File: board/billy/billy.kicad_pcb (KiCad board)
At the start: 2 copper layers, 70 x 50 mm, 83 parts, among them J1 Screw_Terminal_01x02, J10 Screw_Terminal_01x02, J11 Screw_Terminal_01x03, J12 USB_B_Micro, J2 Conn_01x06, J3 Screw_Terminal_01x02, J4 Screw_Terminal_01x02, J5 Conn_01x02, J6 Conn_01x03, J7 Screw_Terminal_01x02, J8 Screw_Terminal_01x02, J9 Screw_Terminal_01x02, Q1 AO3401A, Q2 AO3401A, Q4 AO3400A, Q6 AO3400A, SW1 TS-1088-AR02016, U1 ESP32-S3-WROOM-1, U2 DRV8833PWPR, U3 MAX98357A, U4 DRV8833PWPR, U5 LTC4412, U6 AP63203WU, U7 USBLC6-2SC6

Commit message: Gate Vmotor-sense divider off BOARD_PERIPHERALS_EN (Q7) and merge sensors/status_led into peripherals.c
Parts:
- added Q7: AO3400A, Package_TO_SOT_SMD:SOT-23, F.Cu at (193.5, 82.5)
- moved Q4 2.85 mm to (193.5, 86.2)
- moved R18 2.36 mm to (190.0, 86.2)
- moved Q6 2.06 mm to (188.8, 82.5)
- moved R1 1.42 mm to (171.3, 64.9), turned to -90 degrees
- moved J5 0.40 mm to (174.1, 67.8)
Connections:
- R15 pad 2: GND -> Net-(Q7-D)
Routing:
- net BOOT: track 12.8 -> 7.13 mm, vias 1 -> 0
- net GPIO48: track 30.5 -> 34.5 mm
- net Vmot: track 95.7 -> 92.1 mm
- net Net-(Q7-D): track 0.00 -> 3.11 mm
- net Net-(Q6-D): track 28.6 -> 26.4 mm
- net GPIO14: track 40.0 -> 41.9 mm
- net +3.3V: track 157.2 -> 159.0 mm
- net Net-(D1-VSS): track 9.00 -> 7.49 mm
- net GPIO18: track 36.7 -> 37.6 mm
- net GND: vias 56 -> 59

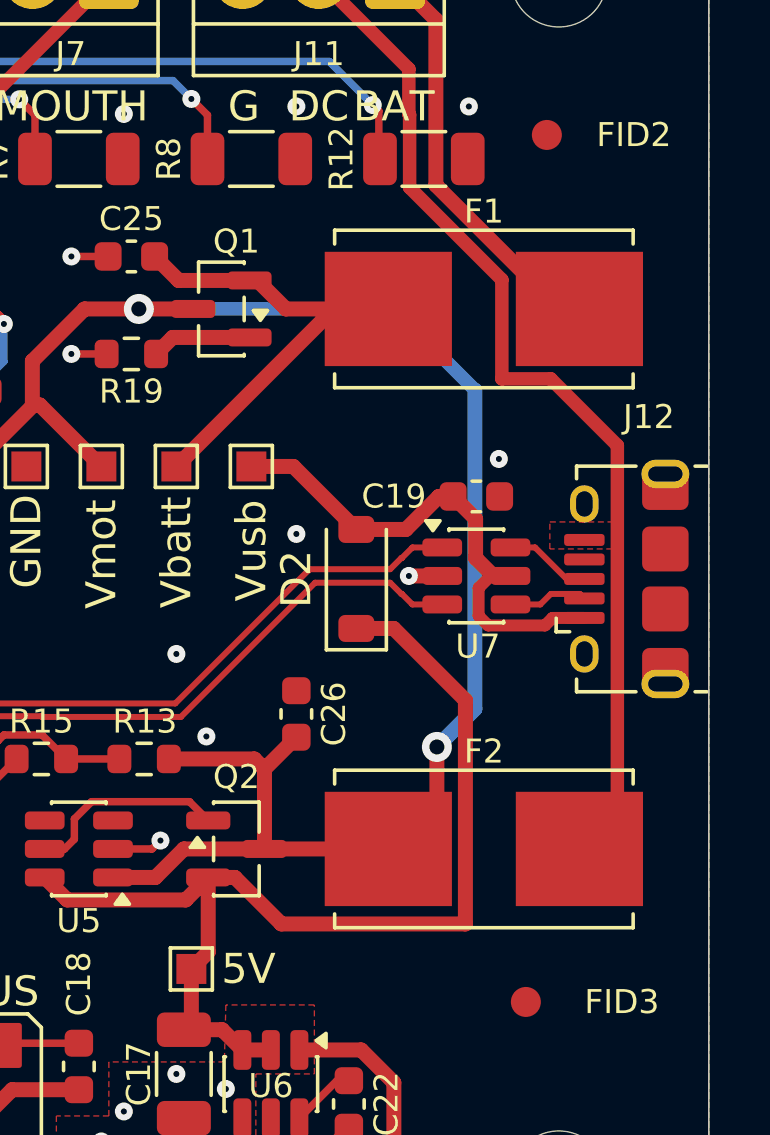
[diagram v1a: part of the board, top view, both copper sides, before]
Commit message: Replace fuse holders with SMD fuses to save cost
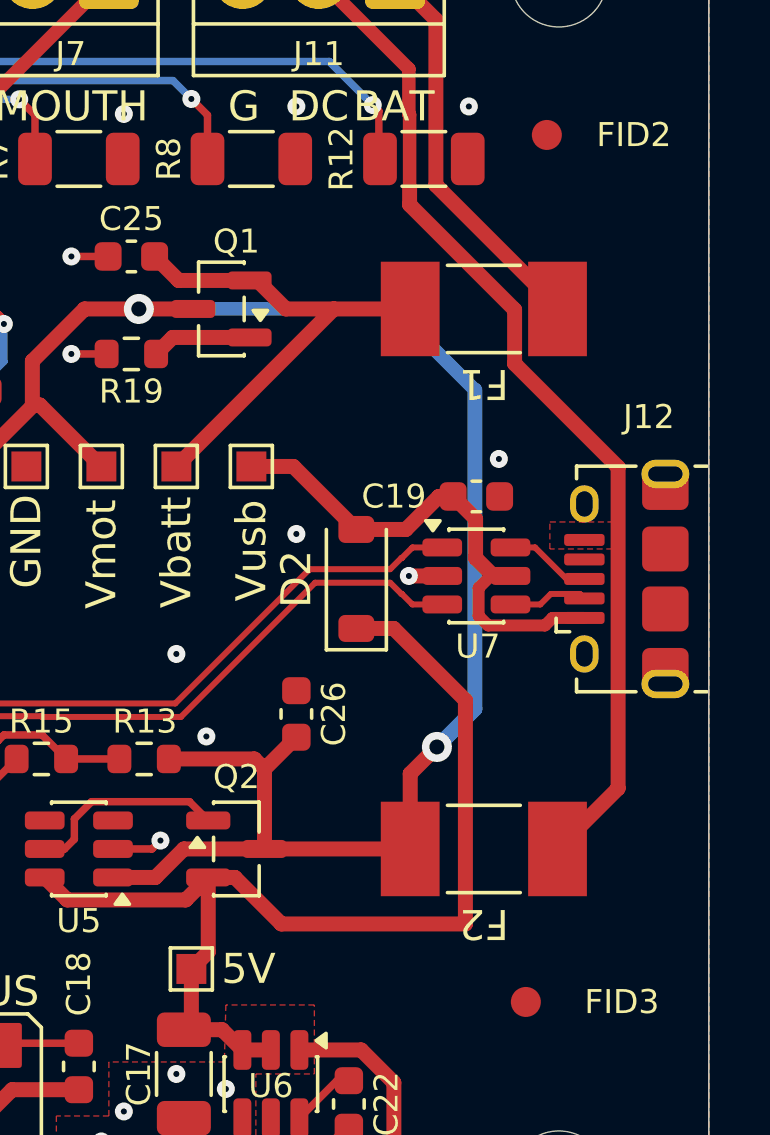
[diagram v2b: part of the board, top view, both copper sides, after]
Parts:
- F1, F2: footprint Fuse:Fuseholder_Littelfuse_Nano2_154x -> Fuse:Fuse_Littelfuse-NANO2-451_453
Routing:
- net Vmot: track 92.1 -> 94.8 mm
- net Net-(J11-Pin_2): track 32.8 -> 34.0 mm
- net Vbatt: track 15.7 -> 16.4 mm

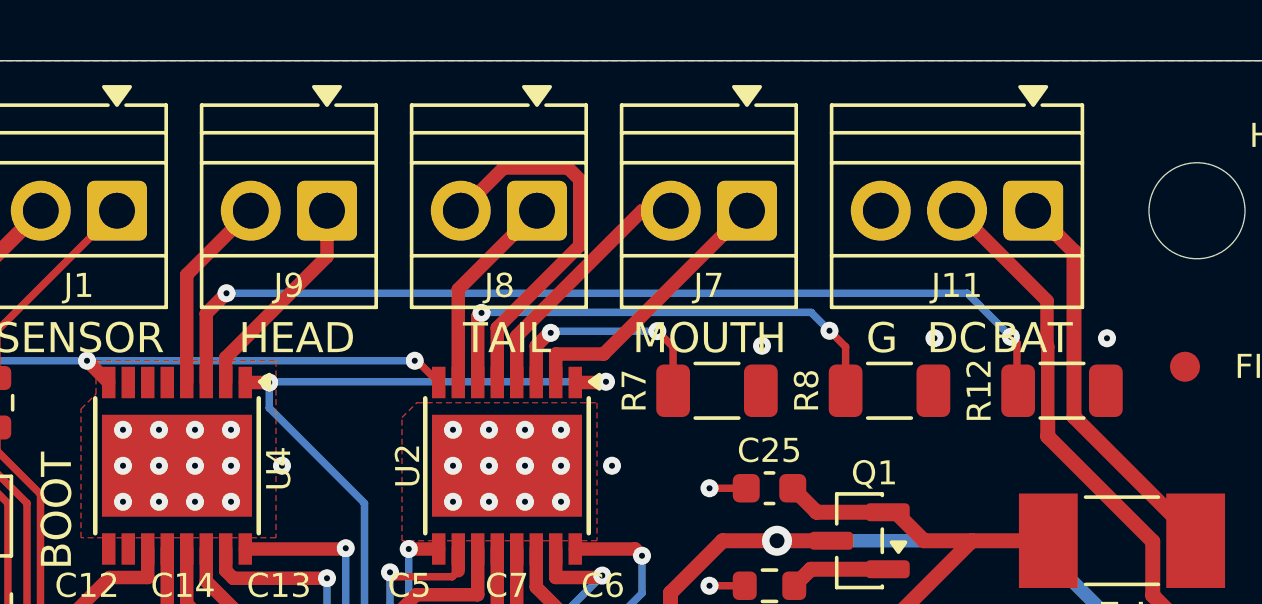
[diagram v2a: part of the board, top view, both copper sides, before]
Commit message: Replace motor screw terminals with 1x6 block to save space and part count
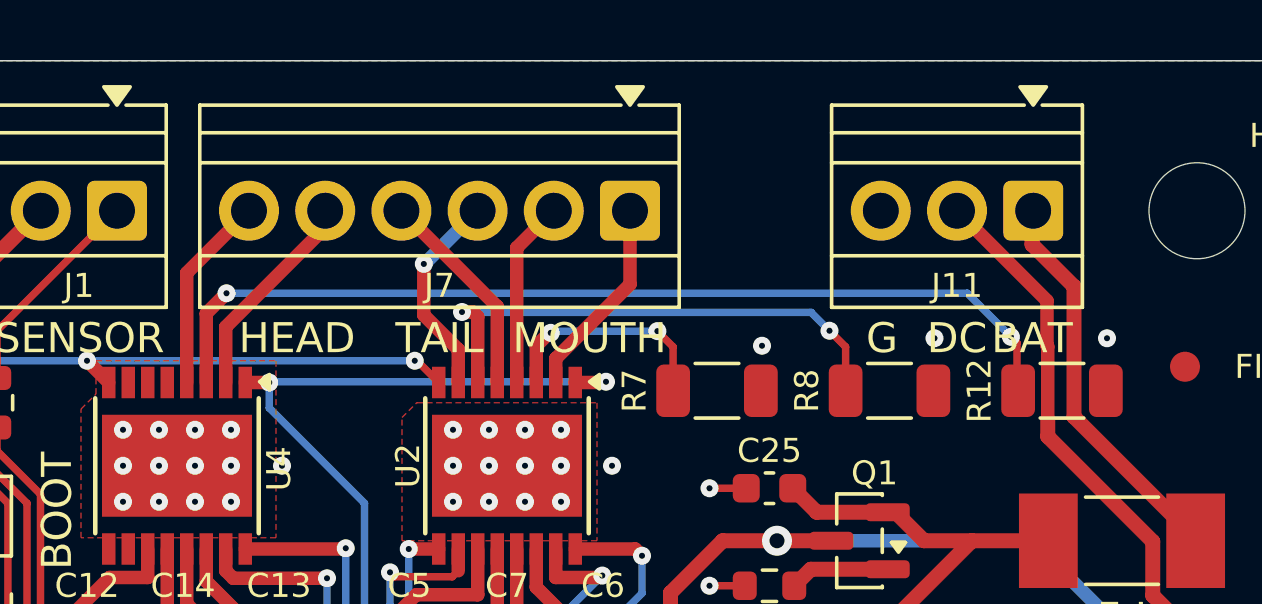
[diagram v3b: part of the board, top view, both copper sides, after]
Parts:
- removed J8, J9: Screw_Terminal_01x02, TerminalBlock:TerminalBlock_Xinya_XY308-2.54-2P_1x02_P2.54mm_Horizontal
- J7: value Screw_Terminal_01x02 -> Screw_Terminal_01x06; footprint TerminalBlock:TerminalBlock_Xinya_XY308-2.54-2P_1x02_P2.54mm_Horizontal -> TerminalBlock:TerminalBlock_Xinya_XY308-2.54-6P_1x06_P2.54mm_Horizontal
- moved J7 3.90 mm to (196.1, 55.0)
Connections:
- U2 pad 5: Net-(J8-Pin_2) -> Net-(J7-Pin_4)
- U2 pad 7: Net-(J8-Pin_1) -> Net-(J7-Pin_3)
- U4 pad 2: Net-(J9-Pin_1) -> Net-(J7-Pin_5)
- U4 pad 4: Net-(J9-Pin_2) -> Net-(J7-Pin_6)
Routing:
- net Net-(J8-Pin_2): track 12.6 -> 0.00 mm
- net Net-(J9-Pin_1): track 7.12 -> 0.00 mm
- net Net-(J7-Pin_4): track 0.00 -> 7.05 mm
- net Net-(J7-Pin_3): track 0.00 -> 6.95 mm, vias 0 -> 1
- net Net-(J8-Pin_1): track 6.81 -> 0.00 mm
- net Net-(J9-Pin_2): track 6.61 -> 0.00 mm
- net Net-(J7-Pin_6): track 0.00 -> 6.58 mm
- net Net-(J7-Pin_5): track 0.00 -> 6.54 mm
- net Net-(J7-Pin_1): track 9.30 -> 6.75 mm
- net Net-(J7-Pin_2): track 8.41 -> 6.24 mm
- net Net-(U2-BISEN): track 16.5 -> 17.5 mm
